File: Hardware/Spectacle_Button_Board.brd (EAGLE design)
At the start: 34 parts, among them J19 FTDI_DEVICE, U1 CY8C4146LQI-S422, U2 MIC5205-5V

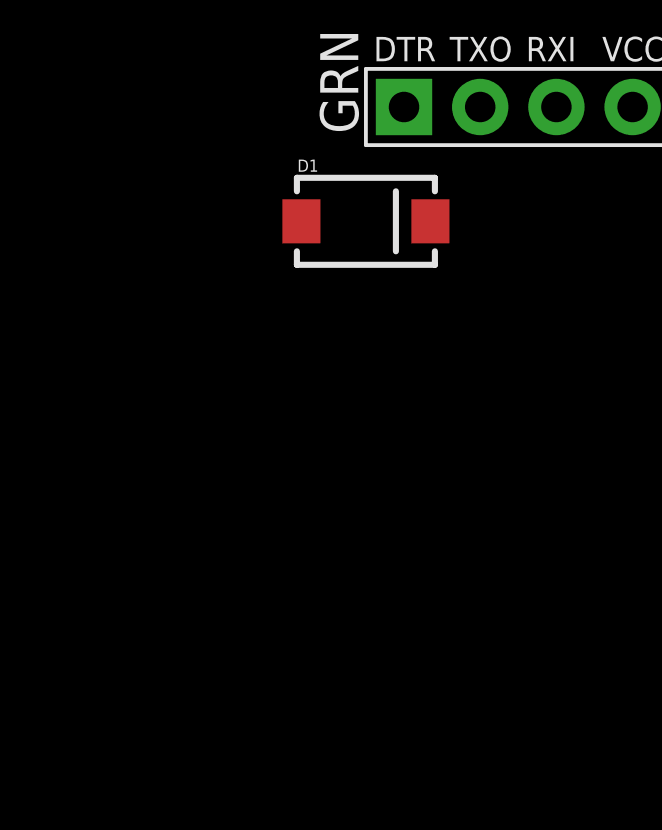
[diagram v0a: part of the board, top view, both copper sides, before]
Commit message: Added LED, buttons
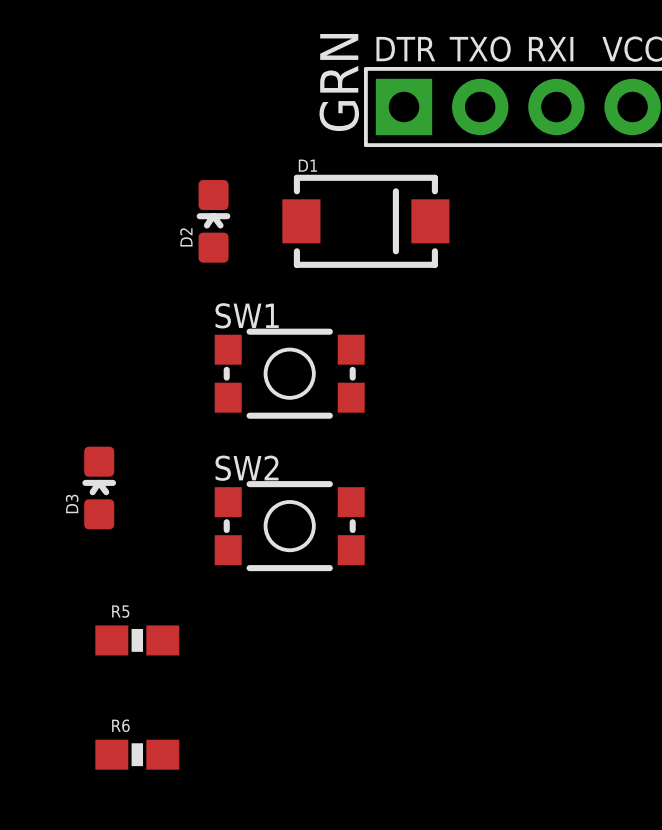
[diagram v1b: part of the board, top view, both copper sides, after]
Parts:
- added D2, D3: RED, SparkFun-LED:LED-0603
- added R5, R6: 1K, SparkFun-Resistors:0603-RES
- added SW1, SW2: (no value), SparkFun-Electromechanical:TACTILE_SWITCH_SMD_4.6X2.8MM
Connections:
- new net BTN: SW2.1, U1.13
- new net LED: R6.2, U1.14
- new net N$4: D2.A, R5.1
- new net N$5: D3.A, R6.1
- net 5V: now also R5.2
- net GND: now also D2.C, D3.C, SW1.3, SW2.3
- net XRES: now also SW1.1
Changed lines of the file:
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@@
 <attribute name="PROD_ID" value="DIO-08053" x="-127" y="-158.75" size="1.778" layer="27" font="vector" ratio="15" display="off"/>
+</element>
+<element name="D2" library="SparkFun-LED" package="LED-0603" value="RED" x="-132.08" y="-158.75">
+<attribute name="PROD_ID" value="DIO-00819" x="-132.08" y="-158.75" size="1.778" layer="27" font="vector" ratio="15" display="off"/>
+</element>
+<element name="SW1" library="SparkFun-Electromechanical" package="TACTILE_SWITCH_SMD_4.6X2.8MM" value="" x="-129.54" y="-163.83">
+<attribute name="PROD_ID" value="SWCH-13065" x="-129.54" y="-163.83" size="1.778" layer="27" font="vector" ratio="15" display="off"/>
+</element>
+<element name="SW2" library="SparkFun-Electromechanical" package="TACTILE_SWITCH_SMD_4.6X2.8MM" value="" x="-129.54" y="-168.91">
+<attribute name="PROD_ID" value="SWCH-13065" x="-129.54" y="-168.91" size="1.778" layer="27" font="vector" ratio="15" display="off"/>
+</element>
+<element name="D3" library="SparkFun-LED" package="LED-0603" value="RED" x="-135.89" y="-167.64">
+<attribute name="PROD_ID" value="DIO-00819" x="-135.89" y="-167.64" size="1.778" layer="27" font="vector" ratio="15" display="off"/>
+</element>
+<element name="R5" library="SparkFun-Resistors" package="0603-RES" value="1K" x="-134.62" y="-172.72">
+<attribute name="PROD_ID" value="RES-07856" x="-134.62" y="-172.72" size="1.778" layer="27" font="vector" ratio="15" display="off"/>
+</element>
+<element name="R6" library="SparkFun-Resistors" package="0603-RES" value="1K" x="-134.62" y="-176.53">
+<attribute name="PROD_ID" value="RES-07856" x="-134.62" y="-176.53" size="1.778" layer="27" font="vector" ratio="15" display="off"/>
 </element>
 </elements>
@@
 <contactref element="J19" pad="P$6"/>
 <contactref element="J19" pad="P$5"/>
+<contactref element="D3" pad="C"/>
+<contactref element="SW2" pad="3"/>
+<contactref element="D2" pad="C"/>
+<contactref element="SW1" pad="3"/>
 <wire x1="-123.61" y1="-125.73" x2="-123.88" y2="-129.54" width="0" layer="19" extent="1-1"/>
 <wire x1="-123.88" y1="-121.92" x2="-123.61" y2="-125.73" width="0" layer="19" extent="1-1"/>
@@
 <wire x1="-115.57" y1="-154.94" x2="-124.46" y2="-149.86" width="0" layer="19" extent="1-1"/>
 <wire x1="-113.03" y1="-154.94" x2="-115.57" y2="-154.94" width="0" layer="19" extent="1-1"/>
+<wire x1="-132.08" y1="-157.873" x2="-124.46" y2="-149.86" width="0" layer="19" extent="1-1"/>
+<wire x1="-127.49" y1="-163.03" x2="-132.08" y2="-157.873" width="0" layer="19" extent="1-1"/>
+<wire x1="-127.49" y1="-168.11" x2="-127.49" y2="-163.03" width="0" layer="19" extent="1-1"/>
+<wire x1="-135.89" y1="-166.763" x2="-127.49" y2="-168.11" width="0" layer="19" extent="1-1"/>
 <wire x1="-20.28" y1="12.95" x2="-123.19" y2="-3.81" width="0" layer="19" extent="1-1"/>
 <wire x1="-20.28" y1="13.95" x2="-20.28" y2="12.95" width="0" layer="19" extent="1-1"/>
@@
 <contactref element="JP1" pad="2"/>
 <contactref element="J18" pad="1"/>
+<contactref element="R5" pad="2"/>
 <wire x1="-125.04" y1="-114.3" x2="-125.04" y2="-118.11" width="0" layer="19" extent="1-1"/>
 <wire x1="-125.31" y1="-106.68" x2="-125.04" y2="-114.3" width="0" layer="19" extent="1-1"/>
@@
 <wire x1="-128.27" y1="-142.24" x2="-125.04" y2="-118.11" width="0" layer="19" extent="1-1"/>
 <wire x1="-127" y1="-149.86" x2="-128.27" y2="-142.24" width="0" layer="19" extent="1-1"/>
+<wire x1="-133.77" y1="-172.72" x2="-127" y2="-149.86" width="0" layer="19" extent="1-1"/>
 <wire x1="-125.41" y1="3.8401" x2="-123.61" y2="-102.87" width="0" layer="19" extent="1-1"/>
 <wire x1="-20.28" y1="13.45" x2="-125.41" y2="3.8401" width="0" layer="19" extent="1-1"/>
@@
 <contactref element="R1" pad="1"/>
 <contactref element="J18" pad="3"/>
+<contactref element="SW1" pad="1"/>
 <wire x1="-121.92" y1="-149.86" x2="-125.31" y2="-102.87" width="0" layer="19" extent="1-1"/>
+<wire x1="-131.59" y1="-164.63" x2="-121.92" y2="-149.86" width="0" layer="19" extent="1-1"/>
 <wire x1="-19.53" y1="15.2" x2="-125.31" y2="-102.87" width="0" layer="19" extent="1-1"/>
 </signal>
@@
 <contactref element="U1" pad="22"/>
 </signal>
+<signal name="N$4">
+<contactref element="D2" pad="A"/>
+<contactref element="R5" pad="1"/>
+<wire x1="-132.08" y1="-159.627" x2="-135.47" y2="-172.72" width="0" layer="19" extent="1-1"/>
+</signal>
+<signal name="BTN">
+<contactref element="U1" pad="13"/>
+<contactref element="SW2" pad="1"/>
+<wire x1="-15.28" y1="12.95" x2="-131.59" y2="-169.71" width="0" layer="19" extent="1-1"/>
+</signal>
+<signal name="LED">
+<contactref element="U1" pad="14"/>
+<contactref element="R6" pad="2"/>
+<wire x1="-15.28" y1="13.45" x2="-133.77" y2="-176.53" width="0" layer="19" extent="1-1"/>
+</signal>
+<signal name="N$5">
+<contactref element="R6" pad="1"/>
+<contactref element="D3" pad="A"/>
+<wire x1="-135.89" y1="-168.517" x2="-135.47" y2="-176.53" width="0" layer="19" extent="1-1"/>
+</signal>
 </signals>
